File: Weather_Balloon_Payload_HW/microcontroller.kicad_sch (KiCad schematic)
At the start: 27 parts, among them J3 Conn_01x04, J4 Conn_01x04, J8 XKTF-015-G, U8 STM32F334C8Tx, Y1 12MHz

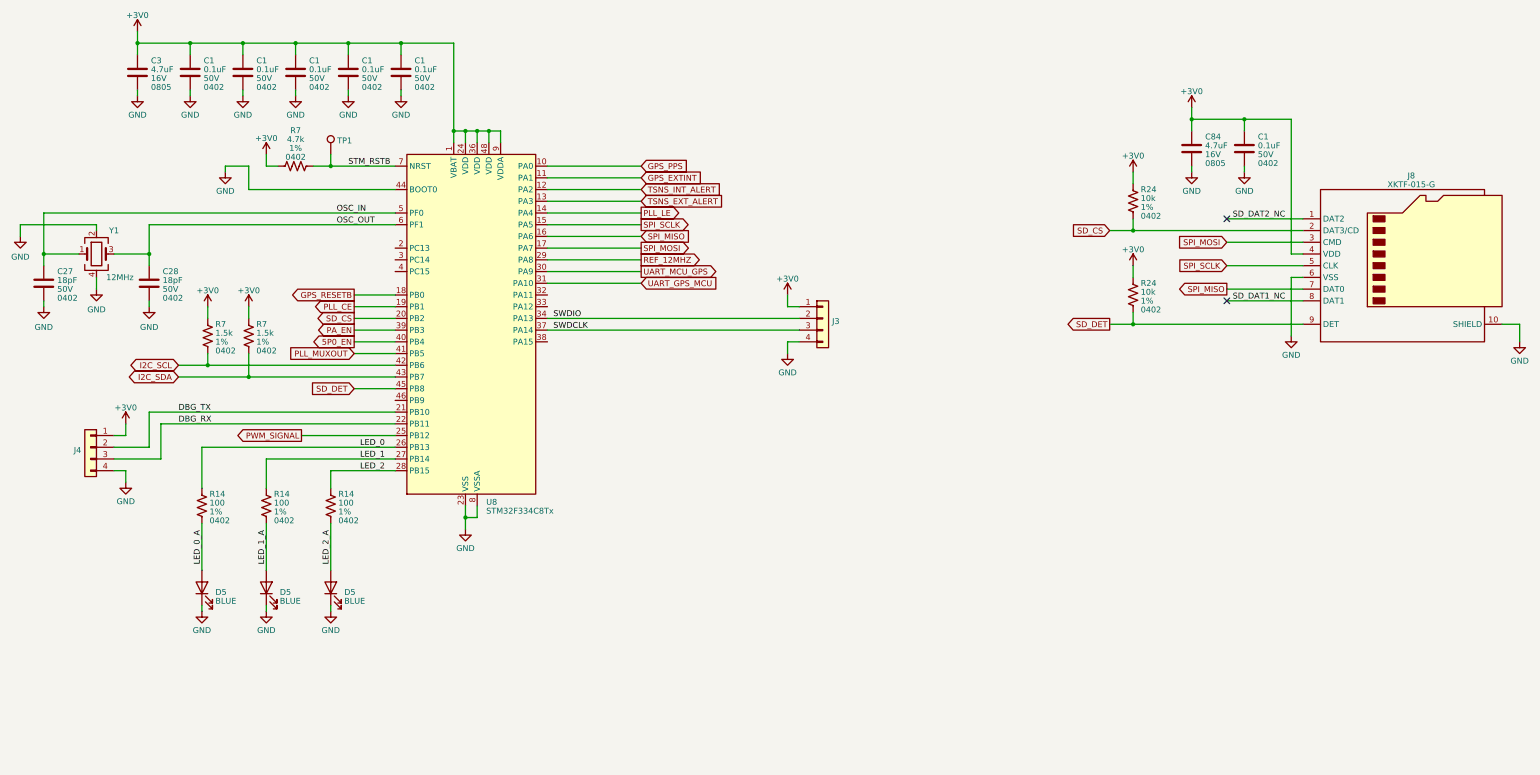
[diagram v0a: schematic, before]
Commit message: Update README, block diagrams, schem. Begin layout
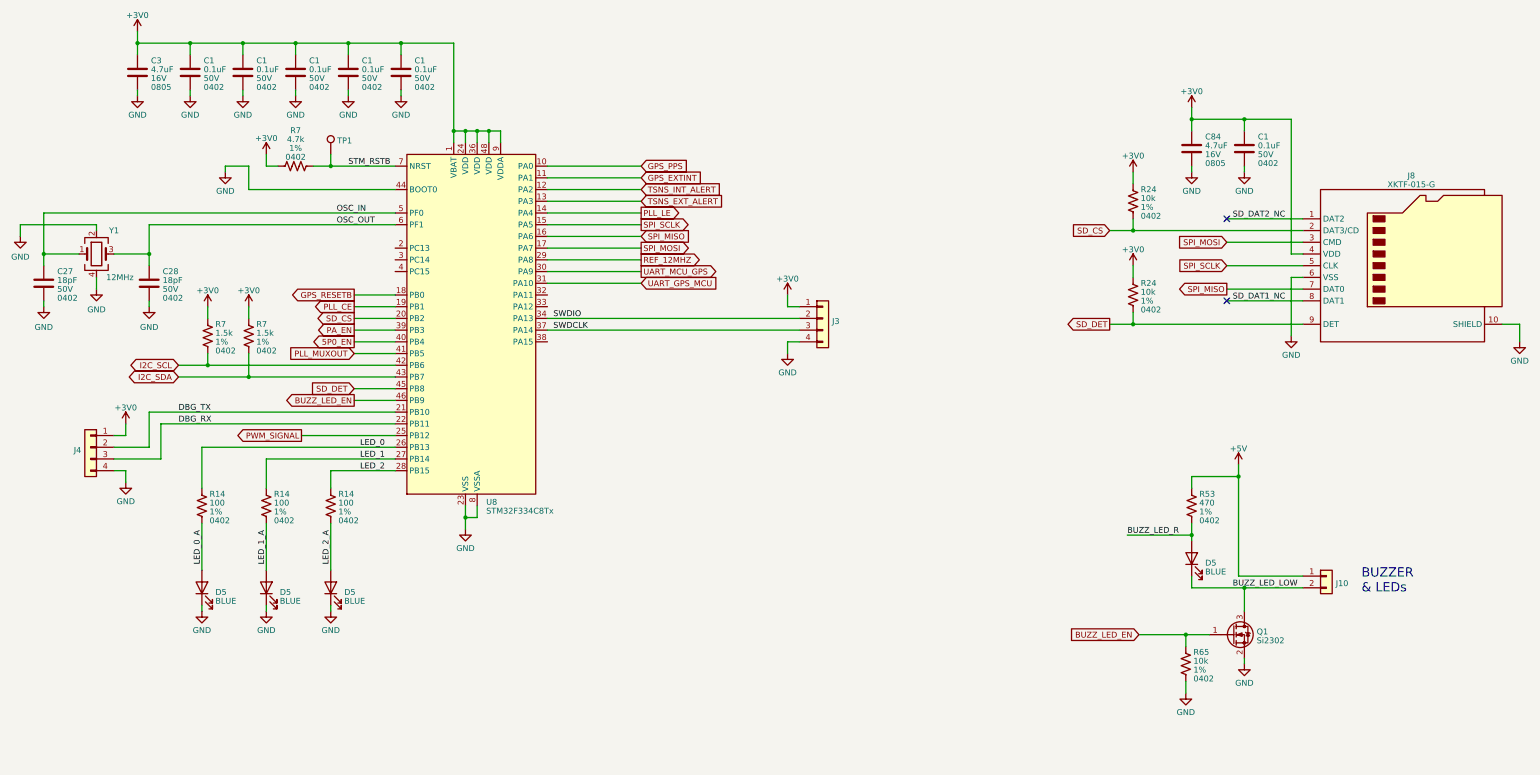
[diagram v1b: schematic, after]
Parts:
- added D5: BLUE, LED_SMD:LED_0402_1005Metric, symbol Device:LED
- added J10: Conn_01x02, Connector_PinHeader_2.54mm:PinHeader_1x02_P2.54mm_Vertical, symbol Connector_Generic:Conn_01x02
- added Q1: Si2302, Repowered_TO-SOT-SMD:SOT-23, symbol Device:Q_NMOS_GSD
- added R53: 470, Resistor_SMD:R_0402_1005Metric, symbol Device:R_US
- added R65: 10k, Resistor_SMD:R_0402_1005Metric, symbol Device:R_US
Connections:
- net GND: now also Q1.2 (S), R65.2
- net BUZZ_LED_EN: now reaches U8.46 (PB9)
- net BUZZ_LED_EN: now also Q1.1 (G), R65.1
- new net +5V: J10.1 (Pin_1), R53.1
- new net BUZZ_LED_LOW: D5.1 (K), J10.2 (Pin_2), Q1.3 (D)
- new net BUZZ_LED_R: D5.2 (A), R53.2
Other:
- note added: "BUZZER & LEDs"

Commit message: Add fabrication files
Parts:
- added J5 (x2): MM8430-2610, Repowered_Connectors:Connector_Murata_MM8430-2610RA1, symbol Repowered_Devices:MM8430-2610
- R53: JLCPCB Part # (none) -> C103054; Manufacturer (none) -> RALEC; Mfr. Part # (none) -> RTT024700FTH
- R7: JLCPCB Part # (none) -> C144726; Manufacturer (none) -> YAGEO; Mfr. Part # (none) -> AC0402JR-071K5L
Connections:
- net GND: now also J5.3 (GND), J5.3 (GND)
- net PWM_SIGNAL: now also J5.1 (IN); no longer U8.25 (PB12)
- new net HRTIM_CHC1: J5.1 (IN), J5.2 (OUT), J5.2 (OUT), U8.25 (PB12)
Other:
- note added: "EXT FREQ IN"
- moved on the sheet: R53
